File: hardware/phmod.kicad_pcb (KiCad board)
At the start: 4 copper layers, 100 x 100 mm, 234 parts, among them J1001 SMA, J1002 SMA, J1003 SMA, J1004 SMA, J101 USB-C, J201 SMA, J202 SMA, J301 SMA, J302 SMA, J303 SMA, J304 SMA, J401 SMA, J402 VM in, J403 coil, J501 SMA, J502 SMA, J503 SMA, J504 SMA, J505 Pmod, J601 SMA, J602 SMA, J701 SMA, J702 SMA, J703 SMA, J704 SMA, J801 SMA, J802 SMA, J803 SMA, J804 SMA, J901 SMA, Q1001 AO3401A, Q1002 2N7002, Q1003 AO3401A, Q1004 AO3400A, Q301 AO3401A, Q401 AO3401A, Q501 AO3401A, Q601 AO3401A, Q701 AO3401A, Q801 AO3401A, Q901 AO3401A, Q902 MMBT3904, SW1001 ON, SW301 ON, SW401 ON, SW501 ON, SW601 ON, SW701 ON, SW801 ON, SW802 DIP4, SW901 ON, U1001 OPA810, U1002 OPA810, U101 TPS65131, U102 LM2664, U201 THS3491, U301 OPA847, U401 DRV8876, U402 OPA810, U501 LMH6629, U502 LMH6629, U601 OPA810, U701 OPA810, U702 OPA810, U901 TPS22917, U902 LMH6629

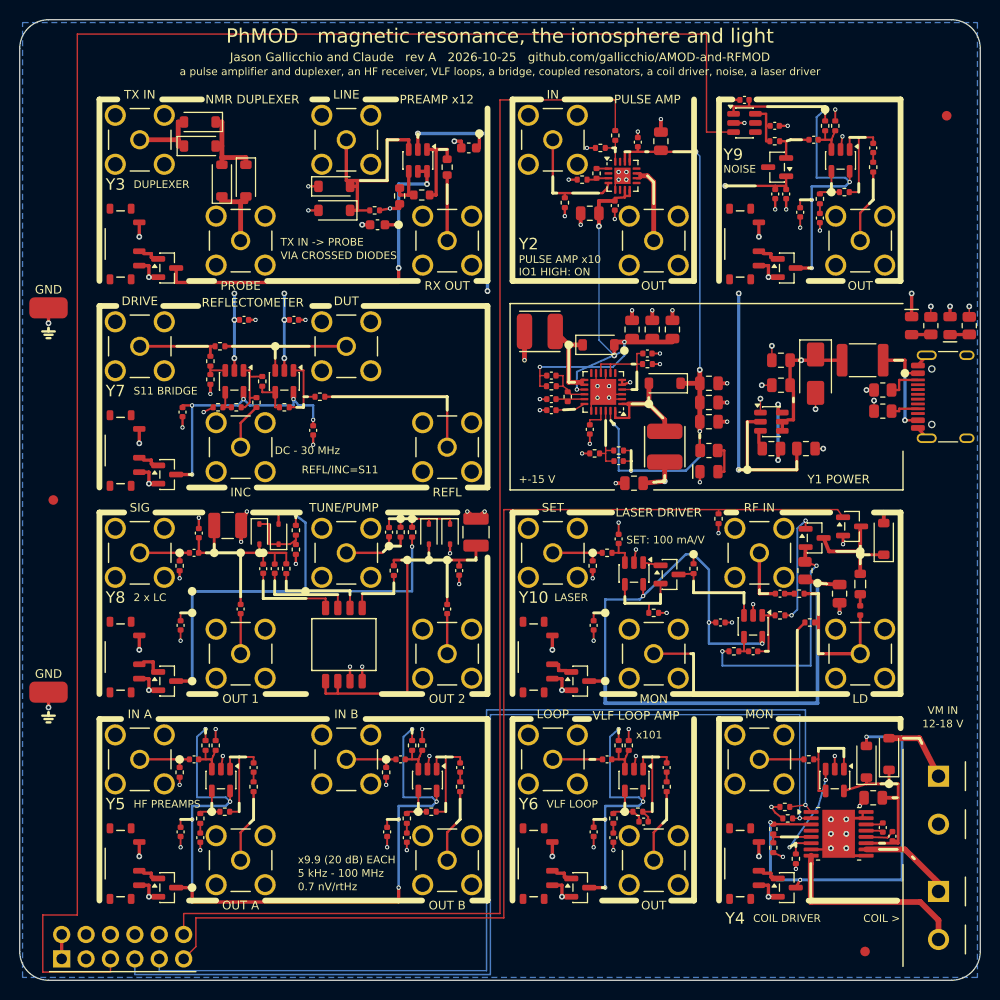
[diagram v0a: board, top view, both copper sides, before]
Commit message: Silk case convention on all six boards (Jason, Prompt 17: "To distinguish whole-tile labels from SMA or port labels, use different cases")
Ports (the jacks' names, terminal and loop names, a port named inside a note) stay UPPER CASE.  A tile's label (its
title on the frame, its name in the corner) is Mixed case: the first letter capitalised and the rest as written ("RC
low-pass", "Synthesizer", "I/Q demodulator"; tiles.label_case).  Ranges, values and notes are lower case except units,
acronyms and part numbers ("loss 1.7 dB", "OUT floats").  RF-MOD-2's X1 and X2 take word titles with their chips in
the info; RF-MOD's and RF-MOD-2's LNA tiles are titled "Preamp" ("Low-noise amp" does not fit a cell's frame); a few
two-line labels moved 0.15-0.3 mm for the descenders mixed case brings.  AMOD-P2's tile records (tile_docs), its DOA
list, KIT.md's AMOD-P2 section; X5's calibration points at P14.  All six boards: ERC 0, DRC 0, all fab checks.

Co-Authored-By: Claude Opus 5.5 <noreply@anthropic.com>
Claude-Session: https://claude.ai/code/session_01RKeoKvFFzjk3cEBLCXXHnB
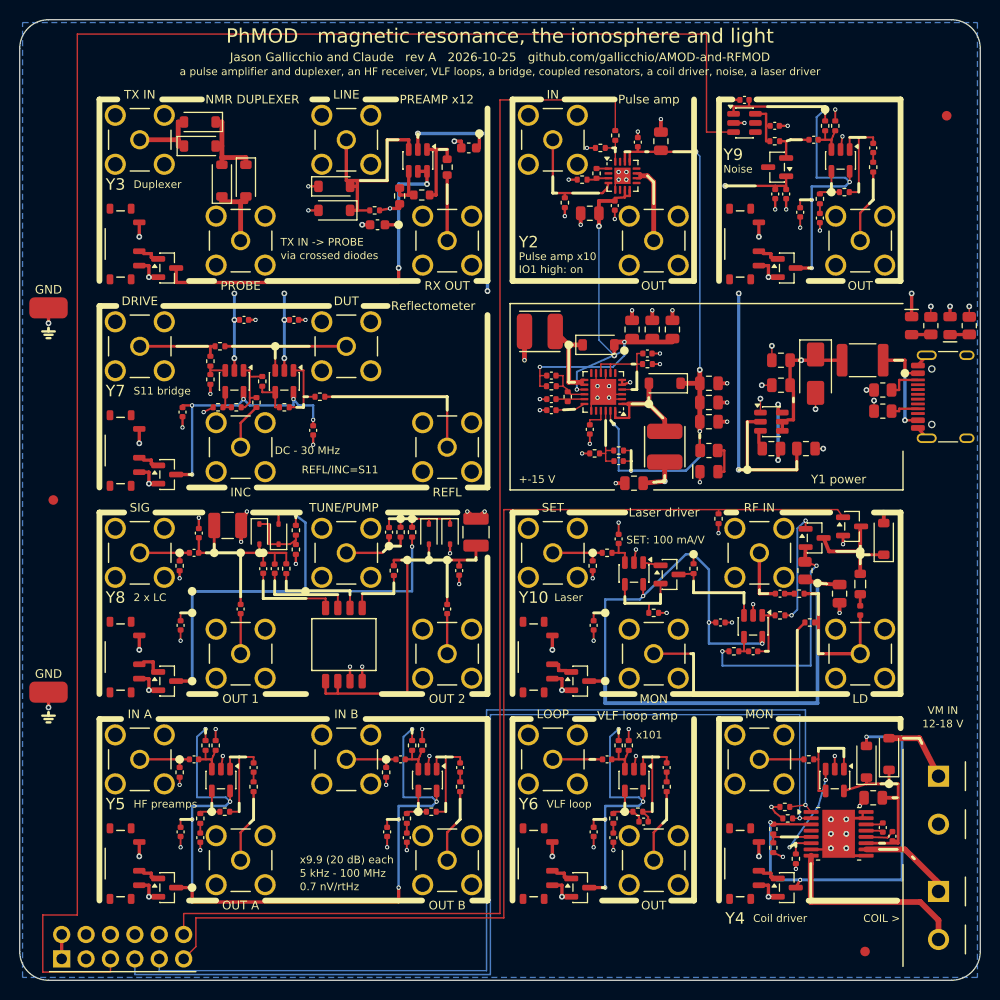
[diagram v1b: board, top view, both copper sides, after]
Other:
- board text added: "Coil driver"
- board text added: "Duplexer"
- board text added: "HF preamps"
- board text added: "IO1 high: on"
- board text added: "Laser"
- board text added: "Laser driver"
- board text added: "Noise"
- board text added: "Pulse amp"
- board text added: "Pulse amp x10"
- board text added: "Reflectometer"
- board text added: "S11 bridge"
- board text added: "VLF loop"
- board text added: "VLF loop amp"
- board text added: "Y1 power"
- board text added: "via crossed diodes"
- board text added: "x9.9 (20 dB) each"
- board text removed: "COIL DRIVER"
- board text removed: "DUPLEXER"
- board text removed: "HF PREAMPS"
- board text removed: "IO1 HIGH: ON"
- board text removed: "LASER"
- board text removed: "LASER DRIVER"
- board text removed: "NOISE"
- board text removed: "PULSE AMP"
- board text removed: "PULSE AMP x10"
- board text removed: "REFLECTOMETER"
- board text removed: "S11 BRIDGE"
- board text removed: "VIA CROSSED DIODES"
- board text removed: "VLF LOOP"
- board text removed: "VLF LOOP AMP"
- board text removed: "Y1 POWER"
- board text removed: "x9.9 (20 dB) EACH"
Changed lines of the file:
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@@
 	(gr_line
 		(start 14.937143 29.8)
-		(end 18.589999 29.8)
+		(end 32.205714 29.8)
 		(stroke
 			(width 0.6)
@@
 	)
 	(gr_line
-		(start 30.45 29.8)
-		(end 32.205714 29.8)
-		(stroke
-			(width 0.6)
-			(type default)
-		)
-		(layer "F.SilkS")
-	)
-	(gr_line
 		(start 32.525 39.25)
 		(end 44.5 39.25)
@@
 	(gr_line
 		(start 35.794286 29.8)
-		(end 48.7 29.8)
+		(end 38.297139 29.8)
 		(stroke
 			(width 0.6)
@@
 	)
 	(gr_line
-		(start 48.7 29.8)
+		(start 48.7 30.7424)
 		(end 48.7 48.7)
 		(stroke
@@
 	(gr_line
 		(start 56.715714 8.3)
-		(end 61.511428 8.3)
+		(end 61.939998 8.3)
 		(stroke
 			(width 0.6)
@@
 	(gr_line
 		(start 57.208572 51.3)
-		(end 61.66857 51.3)
+		(end 63.039999 51.3)
 		(stroke
 			(width 0.6)
@@
 	(gr_line
 		(start 57.787143 72.8)
-		(end 59.282857 72.8)
+		(end 59.754283 72.8)
 		(stroke
 			(width 0.6)
@@
 		(layer "Edge.Cuts")
 	)
-	(gr_text "DUPLEXER"
+	(gr_text "Duplexer"
 		(at 11.85 17.15 0)
 		(layer "F.SilkS")
@@
 		)
 	)
-	(gr_text "S11 BRIDGE"
+	(gr_text "S11 bridge"
 		(at 11.85 38.65 0)
 		(layer "F.SilkS")
@@
 		)
 	)
-	(gr_text "HF PREAMPS"
+	(gr_text "HF preamps"
 		(at 11.85 81.65 0)
 		(layer "F.SilkS")
@@
 		)
 	)
-	(gr_text "VIA CROSSED DIODES"
+	(gr_text "via crossed diodes"
 		(at 27.15 24.55 0)
 		(layer "F.SilkS")
@@
 		)
 	)
-	(gr_text "x9.9 (20 dB) EACH"
-		(at 28.95 87.45 0)
+	(gr_text "x9.9 (20 dB) each"
+		(at 29.15 87.45 0)
 		(layer "F.SilkS")
 		(effects
@@
 	)
 	(gr_text "5 kHz - 100 MHz"
-		(at 28.95 88.85 0)
+		(at 29.15 88.85 0)
 		(layer "F.SilkS")
 		(effects
@@
 	)
 	(gr_text "0.7 nV/rtHz"
-		(at 28.95 90.25 0)
+		(at 29.15 90.25 0)
 		(layer "F.SilkS")
 		(effects
@@
 		)
 	)
-	(gr_text "PULSE AMP x10"
-		(at 51.95 24.95 0)
+	(gr_text "Pulse amp x10"
+		(at 51.95 24.65 0)
 		(layer "F.SilkS")
 		(effects
@@
 		)
 	)
-	(gr_text "IO1 HIGH: ON"
-		(at 51.95 26.25 0)
+	(gr_text "IO1 high: on"
+		(at 51.95 26 0)
 		(layer "F.SilkS")
 		(effects
@@
 		)
 	)
-	(gr_text "VLF LOOP"
+	(gr_text "VLF loop"
 		(at 54.85 81.65 0)
 		(layer "F.SilkS")
@@
 		)
 	)
-	(gr_text "LASER"
+	(gr_text "Laser"
 		(at 55.65 60.15 0)
 		(layer "F.SilkS")
@@
 		)
 	)
-	(gr_text "NOISE"
+	(gr_text "Noise"
 		(at 73.25 15.55 0)
 		(layer "F.SilkS")
@@
 		)
 	)
-	(gr_text "COIL DRIVER"
+	(gr_text "Coil driver"
 		(at 76.35 93.55 0)
 		(layer "F.SilkS")
@@
 		)
 	)
-	(gr_text "Y1 POWER"
+	(gr_text "Y1 power"
 		(at 85.25 47.85 0)
 		(layer "F.SilkS")
@@
 		)
 	)
-	(gr_text "REFLECTOMETER"
-		(at 18.939999 29.45 0)
+	(gr_text "NMR DUPLEXER"
+		(at 19.325715 8.3 0)
 		(layer "F.SilkS")
 		(effects
@@
 		)
 	)
-	(gr_text "NMR DUPLEXER"
-		(at 19.325715 8.3 0)
+	(gr_text "Reflectometer"
+		(at 38.647139 29.8 0)
 		(layer "F.SilkS")
 		(effects
@@
 		)
 	)
-	(gr_text "VLF LOOP AMP"
-		(at 59.632857 72.45 0)
+	(gr_text "VLF loop amp"
+		(at 60.104283 72.45 0)
 		(layer "F.SilkS")
 		(effects
@@
 		)
 	)
-	(gr_text "PULSE AMP"
-		(at 61.861428 8.3 0)
+	(gr_text "Pulse amp"
+		(at 62.289998 8.3 0)
 		(layer "F.SilkS")
 		(effects
@@
 		)
 	)
-	(gr_text "LASER DRIVER"
-		(at 62.01857 51.3 0)
+	(gr_text "Laser driver"
+		(at 63.389999 51.3 0)
 		(layer "F.SilkS")
 		(effects
@@
 	)
 	(gr_text "Y2"
-		(at 51.95 23.35 0)
+		(at 51.95 23.15 0)
 		(layer "F.SilkS")
 		(effects

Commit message: Back-side panels on all six boards; P22 set by hand or by the FPGA; P15 dropped
Jason, Prompt 18: "I hope that the silkscreen (including on the back) is appropriately used to document anything that a
user definitely needs to know to use the tiles successfully and without damaging anything.  If there is additional room
on the back, putting plots of expected responses or other relevant parameters would be great."

- gen_pcb.back_panels: under each tile, mirrored on the back silk, its number and title and the lines in its board's
  BACK dict (levels, loads, supplies, cautions), and where there is one its expected response as a small plot
  (BACK_PLOTS, or the ladder tiles' own simulation; scripts/backplots.py for the rest: amplifiers, datasheet tables,
  the open stub, P23's tuning curve, P10's clipping curve).  A panel goes as one block or in two to four parts, each
  below the one before, clear of the back's tracks and vias where it can be; every panel and plot placed, DRC 0.
- Front silk: Y2 says PULSES ONLY, Y10 "start at mV", R5 and X4 their input level (IN -20 dBm) in place of the noise
  figure.
- P22 (PE43711) on two cells with an 8-way DIP switch: way 1 SPI, ways 2-8 the bits (direct parallel mode with LE pulled
  high), 100 k pull-downs; it still needs the Pmod's 3.3 V.  P15 (two Smith-chart loads) dropped for the cell; P23 moved
  to (3,0).

Co-Authored-By: Claude Opus 5.5 <noreply@anthropic.com>
Claude-Session: https://claude.ai/code/session_01RKeoKvFFzjk3cEBLCXXHnB
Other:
- board text added: "+-10 V, 50 ohm"
- board text added: "+-15 V reach Y2 only"
- board text added: "-5 V 40 mA"
- board text added: "1.3 A limit"
- board text added: "1.6-160 kHz"
- board text added: "100"
- board text added: "10M"
- board text added: "1k"
- board text added: "20 to -20 dB"
- board text added: "300M"
- board text added: "50 to 10 dB"
- board text added: "AT A FEW mV"
- board text added: "DC-30 MHz"
- board text added: "IN max -10 dBm"
- board text added: "IO5 high: off"
- board text added: "IO8 high: on"
- board text added: "LINE: lambda/4"
- board text added: "MON 1.5 V/A"
- board text added: "PULSES ONLY"
- board text added: "PUMP at 2 f"
- board text added: "REFL / INC = S11"
- board text added: "RF IN +10 dBm"
- board text added: "RX OUT x12"
- board text added: "START A LASER"
- board text added: "TUNE: tank 2"
- board text added: "TX IN: from Y2"
- board text added: "USB-C 5 V only"
- board text added: "VCSEL: 30 dB"
- board text added: "VM: 18 V max,"
- board text added: "Y1 Power"
- board text added: "Y10 Laser driver"
- board text added: "Y2 Pulse amp"
- board text added: "Y3 Duplexer and preamp"
- board text added: "Y4 Coil driver"
- board text added: "Y5 HF receiver"
- board text added: "Y6 VLF loop amp"
- board text added: "Y7 Reflectometer"
- board text added: "Y8 Coupled resonators"
- board text added: "Y9 Noise source"
- board text added: "away from mains"
- board text added: "by +-5 %"
- board text added: "cable to probe"
- board text added: "calibrate ENR"
- board text added: "calibrate open, short, load"
- board text added: "duty < 10 %"
- board text added: "else USB 4.6 V"
- board text added: "flat to 50 MHz"
- board text added: "low-pass to the ADC"
- board text added: "never open"
- board text added: "or shorted"
- board text added: "pad on SET"
- board text added: "start at mV"
- board text added: "tanks ~10 MHz"
- board text added: "x9.9 each"
- board text removed: "Pulse amp x10"

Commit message: One letter per board, tiles in lower case: AMOD-P2 is AMOD-N (n1-n11), RF-MOD-2 is IQ-MOD (q1-q11), PhMOD's tiles h1-h10
Jason, Prompt 19: "If we can have a nice, well justified single-letter designator for each board, it would make
everything much more clear", and "d11, q11, and c11 don't look like obvious electronics or PCB things".

- p passive, n networks (AMOD-P2's P14, P16-P25), a active, r radio, h PhMOD (Y1-Y10), q quadrature (RF-MOD-2's X1-X11);
  c, m and b are taken for the conversion, motor and brushless boards to come.  PLAN.md section 13 has the table and
  the reasons (no letter moves to another board, no retired name is reused, no s: s11 is the reflection coefficient).
- Every tile name in lower case on the silk, in the code (Tile ids, BACK/BACK_PLOTS/DOCS keys, the nets built on them),
  the handbooks, README, DOA lists, KIT, PLAN and the review brief; pin names (USB-C A1...), the 4046's R1/C1, nets
  named N1/P1, part numbers ending -R7 and the paper size A1 left alone.  tiles.dump refuses a tile not named
  <letter><n>, a number twice, and a BACK key for a tile that does not exist.
- Board and file renames: boards/amod_n.py, boards/iq_mod.py, docs/DOA_amod_n.md, docs/DOA_iq_mod.md, the handbooks,
  the generated hardware, outputs and pictures.  Silk nudged where a lower-case p or q hung onto the line below.
- All six boards rebuilt: ERC 0, DRC 0, every check.

Co-Authored-By: Claude Opus 5.5 <noreply@anthropic.com>
Claude-Session: https://claude.ai/code/session_01RKeoKvFFzjk3cEBLCXXHnB
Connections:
- net /Y10_G renamed /h10_G
- net /Y10_GA renamed /h10_GA
- net /Y10_GB renamed /h10_GB
- net /Y10_GQ renamed /h10_GQ
- net /Y10_ID renamed /h10_ID
- net /Y10_LDN renamed /h10_LDN
- net /Y10_LM renamed /h10_LM
- net /Y10_MON renamed /h10_MON
- net /Y10_NA renamed /h10_NA
- net /Y10_NS renamed /h10_NS
- net /Y10_REF renamed /h10_REF
- net /Y10_RF renamed /h10_RF
- net /Y10_RFC renamed /h10_RFC
- net /Y10_SET renamed /h10_SET
- net /Y10_SETF renamed /h10_SETF
- net /Y10_SQ renamed /h10_SQ
- net /Y10_VS renamed /h10_VS
- net /Y1_CAPN renamed /h1_CAPN
- net /Y1_CAPP renamed /h1_CAPP
- net /Y1_CC1 renamed /h1_CC1
- net /Y1_CC2 renamed /h1_CC2
- net /Y1_CN renamed /h1_CN
- net /Y1_CP renamed /h1_CP
- net /Y1_FBN renamed /h1_FBN
- net /Y1_FBP renamed /h1_FBP
- net /Y1_LEDG renamed /h1_LEDG
- net /Y1_LEDR renamed /h1_LEDR
- net /Y1_LEDY renamed /h1_LEDY
- net /Y1_SWN renamed /h1_SWN
- net /Y1_SWP renamed /h1_SWP
- net /Y1_VBUS renamed /h1_VBUS
- net /Y1_VINF renamed /h1_VINF
- net /Y1_VREF renamed /h1_VREF
- net /Y2_FBO renamed /h2_FBO
- net /Y2_IN renamed /h2_IN
- net /Y2_INN renamed /h2_INN
- net /Y2_OUT renamed /h2_OUT
- net /Y2_PD renamed /h2_PD
- net /Y3_FB renamed /h3_FB
- net /Y3_G renamed /h3_G
- net /Y3_IN renamed /h3_IN
- net /Y3_M renamed /h3_M
- net /Y3_OUT renamed /h3_OUT
- net /Y3_OUT_A renamed /h3_OUT_A
- net /Y3_PRB renamed /h3_PRB
- net /Y3_TX renamed /h3_TX
- net /Y3_VS renamed /h3_VS
- net /Y4_CPH renamed /h4_CPH
- net /Y4_CPL renamed /h4_CPL
- net /Y4_G renamed /h4_G
- net /Y4_IP renamed /h4_IP
- net /Y4_MO renamed /h4_MO
- net /Y4_MON renamed /h4_MON
- net /Y4_OUT1 renamed /h4_OUT1
- net /Y4_OUT2 renamed /h4_OUT2
- net /Y4_VCP renamed /h4_VCP
- net /Y4_VEXT renamed /h4_VEXT
- net /Y4_VM renamed /h4_VM
- net /Y4_VREF renamed /h4_VREF
- net /Y4_VS renamed /h4_VS
- net /Y5_CG renamed /h5_CG
- net /Y5_CGB renamed /h5_CGB
- net /Y5_FB renamed /h5_FB
- net /Y5_FBB renamed /h5_FBB
- net /Y5_G renamed /h5_G
- net /Y5_IN renamed /h5_IN
- net /Y5_IN2 renamed /h5_IN2
- net /Y5_IN2B renamed /h5_IN2B
- net /Y5_INB renamed /h5_INB
- net /Y5_OA renamed /h5_OA
- net /Y5_OAB renamed /h5_OAB
- net /Y5_OC renamed /h5_OC
- net /Y5_OCB renamed /h5_OCB
- net /Y5_OUT renamed /h5_OUT
- net /Y5_OUTB renamed /h5_OUTB
- net /Y5_VS renamed /h5_VS
- net /Y6_CG renamed /h6_CG
- net /Y6_FB renamed /h6_FB
- net /Y6_G renamed /h6_G
- net /Y6_IN renamed /h6_IN
- net /Y6_IN2 renamed /h6_IN2
- net /Y6_OA renamed /h6_OA
- net /Y6_OC renamed /h6_OC
- net /Y6_OUT renamed /h6_OUT
- net /Y6_VS renamed /h6_VS
- net /Y7_A renamed /h7_A
- net /Y7_B renamed /h7_B
- net /Y7_DRV renamed /h7_DRV
- net /Y7_G renamed /h7_G
- net /Y7_INC renamed /h7_INC
- net /Y7_N1 renamed /h7_N1
- net /Y7_N2 renamed /h7_N2
- net /Y7_O1 renamed /h7_O1
- net /Y7_O2 renamed /h7_O2
- net /Y7_REFL renamed /h7_REFL
- net /Y7_VS renamed /h7_VS
- net /Y8_CA renamed /h8_CA
- net /Y8_CB renamed /h8_CB
- net /Y8_G renamed /h8_G
- net /Y8_K1 renamed /h8_K1
- net /Y8_K2 renamed /h8_K2
- net /Y8_OUT1 renamed /h8_OUT1
- net /Y8_OUT2 renamed /h8_OUT2
- net /Y8_RDA renamed /h8_RDA
- net /Y8_RDB renamed /h8_RDB
- net /Y8_SIG renamed /h8_SIG
- net /Y8_T1 renamed /h8_T1
- net /Y8_T2 renamed /h8_T2
- net /Y8_TP renamed /h8_TP
- net /Y8_VS renamed /h8_VS
- net /Y9_CG renamed /h9_CG
- net /Y9_FB renamed /h9_FB
- net /Y9_G renamed /h9_G
- net /Y9_IN renamed /h9_IN
- net /Y9_IN2 renamed /h9_IN2
- net /Y9_OA renamed /h9_OA
- net /Y9_OC renamed /h9_OC
- net /Y9_OUT renamed /h9_OUT
- net /Y9_VN renamed /h9_VN
- net /Y9_VS renamed /h9_VS
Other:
- board text added: "+-15 V reach h2 only"
- board text added: "TX IN: from h2"
- board text added: "h1 Power"
- board text added: "h1 power"
- board text added: "h10"
- board text added: "h10 Laser driver"
- board text added: "h2"
- board text added: "h2 Pulse amp"
- board text added: "h3"
- board text added: "h3 Duplexer and preamp"
- board text added: "h4"
- board text added: "h4 Coil driver"
- board text added: "h5"
- board text added: "h5 HF receiver"
- board text added: "h6"
- board text added: "h6 VLF loop amp"
- board text added: "h7"
- board text added: "h7 Reflectometer"
- board text added: "h8"
- board text added: "h8 Coupled resonators"
- board text added: "h9"
- board text added: "h9 Noise source"
- board text added: "tiles have a slide switch (up: on). USB-C on h1. h2"
- board text removed: "+-15 V reach Y2 only"
- board text removed: "TX IN: from Y2"
- board text removed: "Y1 Power"
- board text removed: "Y1 power"
- board text removed: "Y10"
- board text removed: "Y10 Laser driver"
- board text removed: "Y2"
- board text removed: "Y2 Pulse amp"
- board text removed: "Y3"
- board text removed: "Y3 Duplexer and preamp"
- board text removed: "Y4"
- board text removed: "Y4 Coil driver"
- board text removed: "Y5"
- board text removed: "Y5 HF receiver"
- board text removed: "Y6"
- board text removed: "Y6 VLF loop amp"
- board text removed: "Y7"
- board text removed: "Y7 Reflectometer"
- board text removed: "Y8"
- board text removed: "Y8 Coupled resonators"
- board text removed: "Y9"
- board text removed: "Y9 Noise source"
- board text removed: "tiles have a slide switch (up: on). USB-C on Y1. Y2"
